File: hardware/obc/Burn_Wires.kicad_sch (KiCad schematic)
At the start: 28 parts, among them Q501 MMBT2222AT, Q502 IRLML2803, Q503 IRLML2803, Q504 IRLML2803, Q505 IRF7406PbF, Q506 IRF7406PbF, Q507 IRF7406PbF, U501 PE014006

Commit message: obc: design review 5/28 implemented
Entered step models, adjusted pin clearances, and edited footprints.
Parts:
- D501: footprint mainboard:PWRDI-123 -> Diode_SMD:D_SOD-123
- U501: footprint mainboard:RELAY_PE014006 -> SSE_Footprints:RELAY_PE014006_REV-SSE
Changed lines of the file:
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@@
 			)
 		)
-		(property "Footprint" "mainboard:PWRDI-123"
+		(property "Footprint" "Diode_SMD:D_SOD-123"
 			(at 58.42 35.56 0)
 			(effects
@@
 			)
 		)
-		(property "Footprint" "mainboard:RELAY_PE014006"
+		(property "Footprint" "SSE_Footprints:RELAY_PE014006_REV-SSE"
 			(at 81.28 33.02 0)
 			(effects

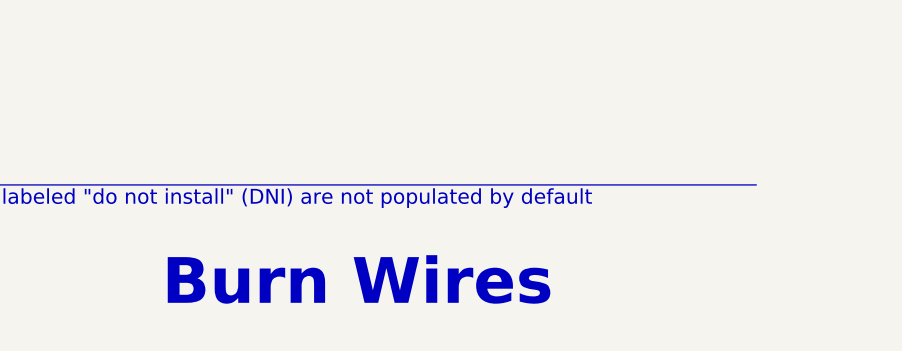
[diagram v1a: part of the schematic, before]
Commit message: obc: power connection cleanup
Decreased track length to vias and centered all vias in pad. Updated schematic title blocks, edited 3D models.
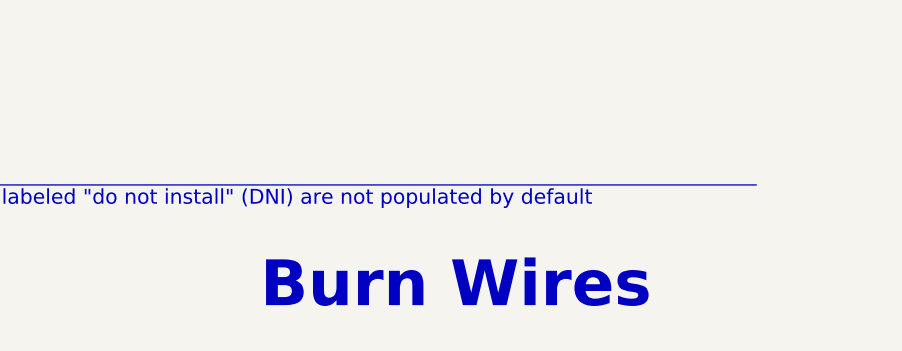
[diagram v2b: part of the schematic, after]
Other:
- company: Max Holliday -> Ruchir Kavulli, Michael Lyle
- title: PyCubed Mainboard -> Obi Wan Komputer
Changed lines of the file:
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@@
 	(paper "USLetter")
 	(title_block
-		(title "PyCubed Mainboard")
-		(date "2021-06-09")
-		(rev "v05c")
-		(company "Max Holliday")
+		(title "Obi Wan Komputer")
+		(date "2024-06-07")
+		(rev "vA")
+		(company "Ruchir Kavulli, Michael Lyle")
+		(comment 1 "Derived from PyCubed Mainboard v5")
 	)
 	(junction
@@
 	(text "Burn Wires"
 		(exclude_from_sim no)
-		(at 200.66 182.88 0)
+		(at 211.582 183.134 0)
 		(effects
 			(font

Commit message: obc: test traces for high priority signals
Preliminary trace creation for high priority signals.
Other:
- title: Obi Wan Komputer -> Obi Wan Computer
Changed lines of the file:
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@@
 	(paper "USLetter")
 	(title_block
-		(title "Obi Wan Komputer")
+		(title "Obi Wan Computer")
 		(date "2024-06-07")
 		(rev "vA")

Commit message: obc: free angle test routing
Re-routed several nets using free angle mode, aiming to reduce trace length and increase space between traces.
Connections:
- net VBATT: now also D501.1; no longer D501.C
- net at Q501.3 (C), U501.5 (A2): now also D501.2; no longer D501.A
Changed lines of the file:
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@@
 			)
 		)
-		(pin "A"
+		(pin "2"
 		)
-		(pin "C"
+		(pin "1"
 		)
 		(instances

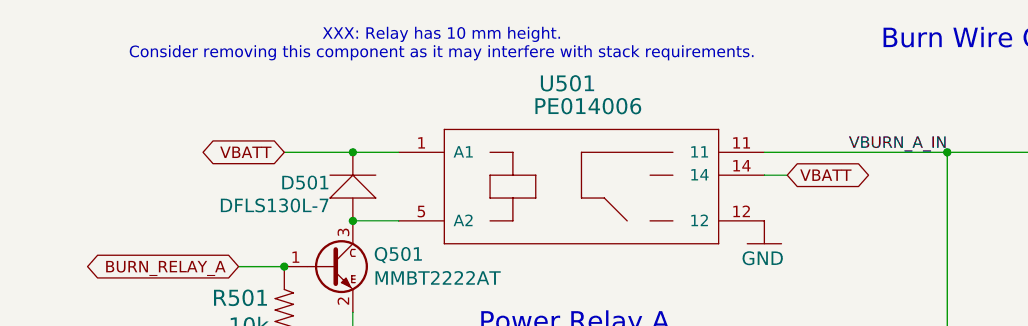
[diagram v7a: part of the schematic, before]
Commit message: obc: remove superfluous schem XXX comments
All were reviewed.

- Some didn't matter - entire comment removed
- Some were just notes, not action items - XXX notation removed

Two items noted do have implications, though:

- WDT rst pulldown value is incorrect.
- I2C pulls are missing (though this could be ignored).
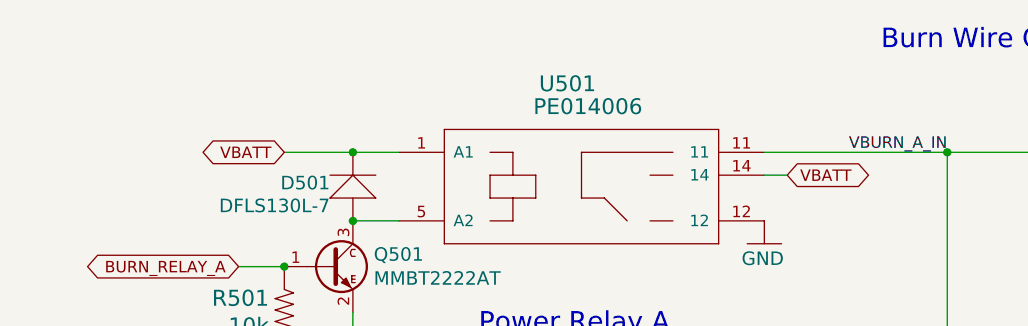
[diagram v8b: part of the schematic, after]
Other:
- note removed: "XXX: Relay has 10 mm height. Consider removing this component as it may interfere with stack requirements."
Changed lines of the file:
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@@
-		)
-	)
-	(text "XXX: Relay has 10 mm height.\nConsider removing this component as it may interfere with stack requirements."
-		(exclude_from_sim no)
-		(at 68.326 18.542 0)
-		(effects
-			(font
-				(size 1.27 1.27)
-			)
 		)
 	)
